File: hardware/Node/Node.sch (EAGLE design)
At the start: 67 parts, among them J1 AVR_SPI_PRG_6NS, J2 M04X2, Q1 PMR280UN, Q2 PMR280UN, Q3 PMR280UN, SW1 KSS, SW2 KSS, U1 ATMEGA32U4QFN, U2 BLUETOOTH-RN41", U3 LSM303DLM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

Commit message: move stuff to meet the DRC
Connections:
- net GND: now also HWB.3; no longer HWB.1
- net HWB: now also HWB.1; no longer HWB.3
- net PROG2: now also U1.PB7; no longer U1.PB0(SS)
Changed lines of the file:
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@@
 <instance part="SW1" gate="G$1" x="160.02" y="154.94" rot="MR0"/>
 <instance part="SW2" gate="G$1" x="160.02" y="144.78"/>
-<instance part="HWB" gate="G$1" x="48.26" y="134.62" smashed="yes">
-<attribute name="NAME" x="45.72" y="140.97" size="1.778" layer="95"/>
+<instance part="HWB" gate="G$1" x="48.26" y="134.62" smashed="yes" rot="MR0">
+<attribute name="NAME" x="50.8" y="140.97" size="1.778" layer="95" rot="MR0"/>
 </instance>
 <instance part="POWER" gate="1" x="129.54" y="187.96"/>
@@
 <junction x="66.04" y="127"/>
 <wire x1="30.48" y1="127" x2="43.18" y2="127" width="0.1524" layer="91"/>
-<pinref part="HWB" gate="G$1" pin="1"/>
+<pinref part="HWB" gate="G$1" pin="3"/>
 <wire x1="43.18" y1="127" x2="66.04" y2="127" width="0.1524" layer="91"/>
 <wire x1="43.18" y1="134.62" x2="43.18" y2="127" width="0.1524" layer="91"/>
@@
 <segment>
 <wire x1="58.42" y1="134.62" x2="55.88" y2="134.62" width="0.1524" layer="91"/>
-<pinref part="HWB" gate="G$1" pin="3"/>
 <label x="55.88" y="134.62" size="1.778" layer="95"/>
 <pinref part="R18" gate="G$1" pin="1"/>
-<wire x1="55.88" y1="134.62" x2="53.34" y2="134.62" width="0.1524" layer="91"/>
+<pinref part="HWB" gate="G$1" pin="1"/>
+<wire x1="53.34" y1="134.62" x2="55.88" y2="134.62" width="0.1524" layer="91"/>
 <junction x="55.88" y="134.62"/>
 </segment>
@@
 </segment>
 <segment>
-<pinref part="U1" gate="G$1" pin="PB0(SS)"/>
-<wire x1="139.7" y1="76.2" x2="144.78" y2="76.2" width="0.1524" layer="91"/>
-<label x="144.78" y="76.2" size="1.778" layer="95"/>
-</segment>
-</net>
+<pinref part="U1" gate="G$1" pin="PB7"/>
+<wire x1="139.7" y1="83.82" x2="144.78" y2="83.82" width="0.1524" layer="91"/>
+<label x="144.78" y="83.82" size="1.778" layer="95"/>
+</segment>
+</net>

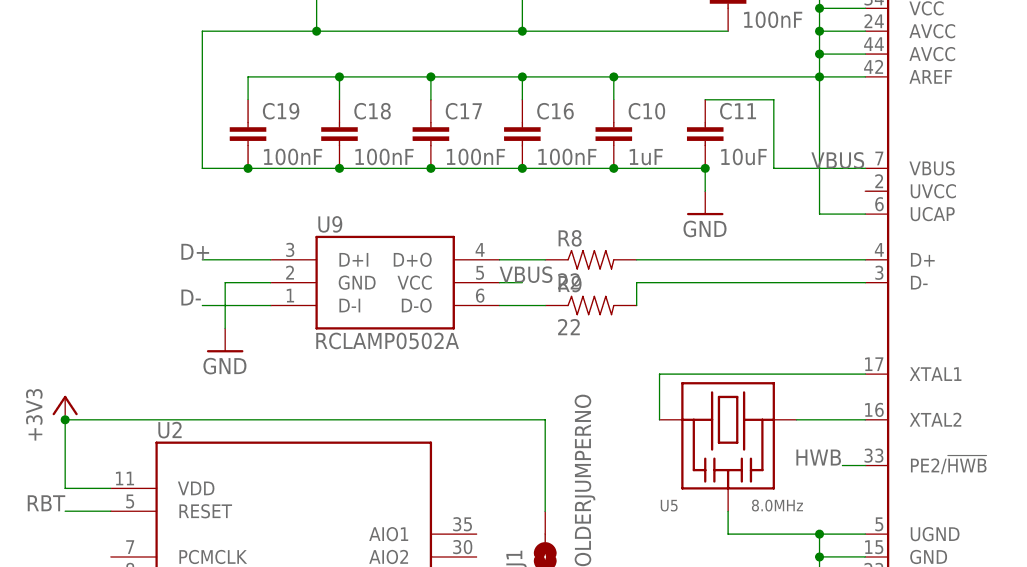
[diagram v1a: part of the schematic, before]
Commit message: fix packages, route ISP
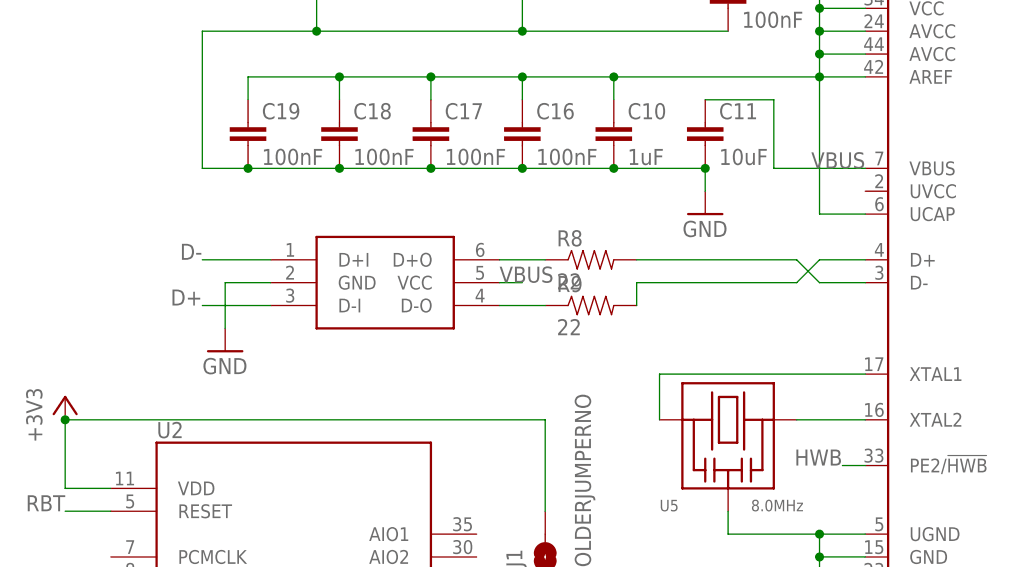
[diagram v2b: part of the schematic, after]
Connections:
- removed net N$23: R8.2, U1.D+
- new net N$15: R8.2, U1.D-
- net D+: now also U9.D-I; no longer U9.D+I
- net D-: now also U9.D+I; no longer U9.D-I
- net N$24: now also U1.D+; no longer U1.D-
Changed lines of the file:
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@@
 </segment>
 </net>
-<net name="N$23" class="0">
-<segment>
-<pinref part="R8" gate="G$1" pin="2"/>
+<net name="N$24" class="0">
+<segment>
+<pinref part="R9" gate="G$1" pin="2"/>
+<wire x1="78.74" y1="99.06" x2="78.74" y2="96.52" width="0.1524" layer="91"/>
+<wire x1="78.74" y1="99.06" x2="96.52" y2="99.06" width="0.1524" layer="91"/>
+<wire x1="96.52" y1="99.06" x2="99.06" y2="101.6" width="0.1524" layer="91"/>
 <pinref part="U1" gate="G$1" pin="D+"/>
-<wire x1="78.74" y1="101.6" x2="104.14" y2="101.6" width="0.1524" layer="91"/>
-</segment>
-</net>
-<net name="N$24" class="0">
-<segment>
-<pinref part="U1" gate="G$1" pin="D-"/>
-<pinref part="R9" gate="G$1" pin="2"/>
-<wire x1="104.14" y1="99.06" x2="78.74" y2="99.06" width="0.1524" layer="91"/>
-<wire x1="78.74" y1="99.06" x2="78.74" y2="96.52" width="0.1524" layer="91"/>
+<wire x1="99.06" y1="101.6" x2="104.14" y2="101.6" width="0.1524" layer="91"/>
 </segment>
 </net>
@@
 </segment>
 <segment>
-<wire x1="38.1" y1="96.52" x2="30.48" y2="96.52" width="0.1524" layer="91"/>
-<label x="27.94" y="96.52" size="1.778" layer="95"/>
-<pinref part="U9" gate="G$1" pin="D-I"/>
+<pinref part="U9" gate="G$1" pin="D+I"/>
+<wire x1="38.1" y1="101.6" x2="30.48" y2="101.6" width="0.1524" layer="91"/>
+<label x="30.48" y="101.6" size="1.778" layer="95" rot="MR0"/>
 </segment>
 </net>
@@
 </segment>
 <segment>
-<wire x1="38.1" y1="101.6" x2="30.48" y2="101.6" width="0.1524" layer="91"/>
-<label x="27.94" y="101.6" size="1.778" layer="95"/>
-<pinref part="U9" gate="G$1" pin="D+I"/>
+<pinref part="U9" gate="G$1" pin="D-I"/>
+<wire x1="38.1" y1="96.52" x2="30.48" y2="96.52" width="0.1524" layer="91"/>
+<label x="30.48" y="96.52" size="1.778" layer="95" rot="MR0"/>
 </segment>
 </net>
@@
 </segment>
 </net>
+<net name="N$15" class="0">
+<segment>
+<pinref part="R8" gate="G$1" pin="2"/>
+<wire x1="78.74" y1="101.6" x2="96.52" y2="101.6" width="0.1524" layer="91"/>
+<wire x1="96.52" y1="101.6" x2="99.06" y2="99.06" width="0.1524" layer="91"/>
+<pinref part="U1" gate="G$1" pin="D-"/>
+<wire x1="99.06" y1="99.06" x2="104.14" y2="99.06" width="0.1524" layer="91"/>
+</segment>
+</net>

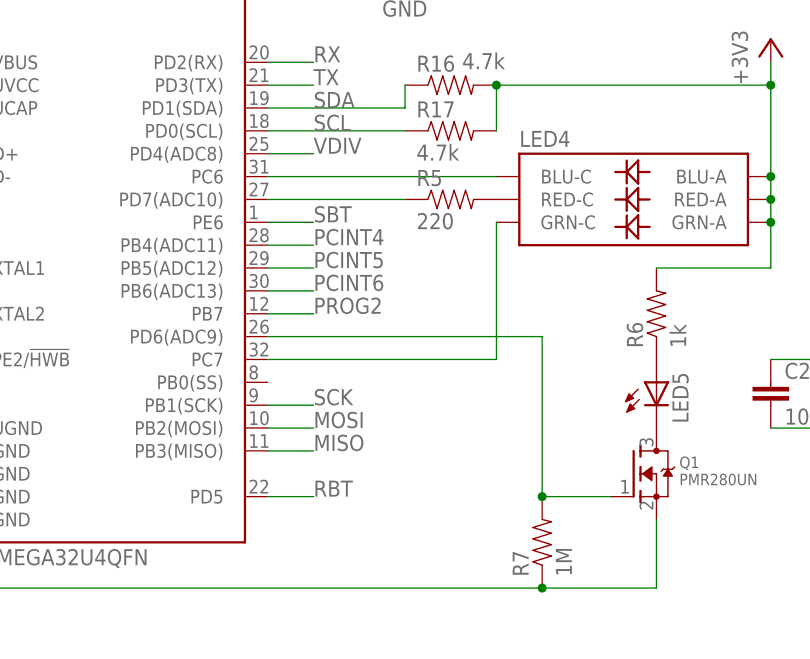
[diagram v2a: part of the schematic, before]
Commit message: route LEDs and interrupts
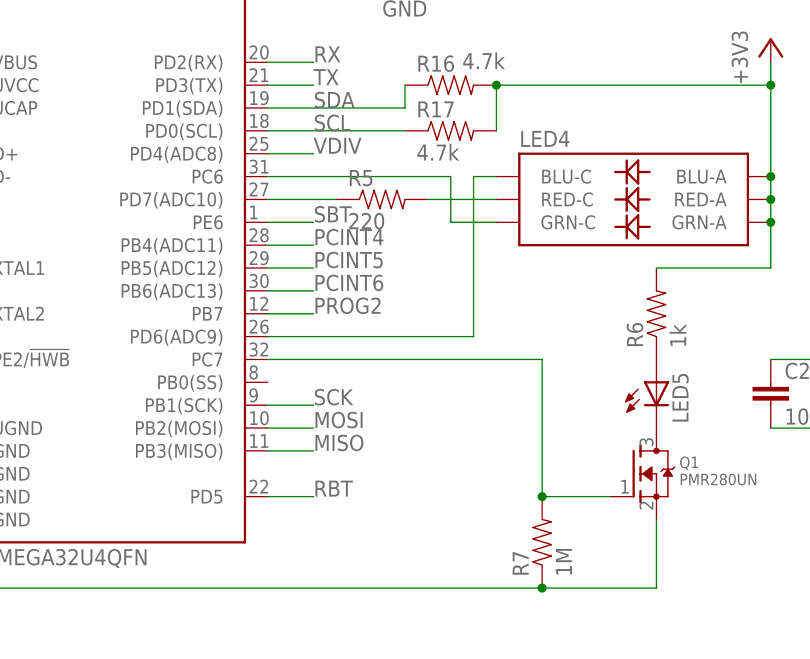
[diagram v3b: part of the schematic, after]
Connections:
- net N$12: now also LED4.GRN-C; no longer LED4.BLU-C
- net N$17: now also LED4.BLU-C, U1.PD6(ADC9); no longer LED4.GRN-C, U1.PC7
- net N$22: now also U1.PC7; no longer U1.PD6(ADC9)
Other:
- moved on the sheet: R5
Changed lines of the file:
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@@
 <grid distance="0.1" unitdist="inch" unit="inch" style="lines" multiple="1" display="no" altdistance="0.01" altunitdist="inch" altunit="inch"/>
 <layers>
-<layer number="1" name="Top" color="4" fill="1" visible="no" active="no"/>
-<layer number="16" name="Bottom" color="1" fill="1" visible="no" active="no"/>
-<layer number="17" name="Pads" color="2" fill="1" visible="no" active="no"/>
-<layer number="18" name="Vias" color="2" fill="1" visible="no" active="no"/>
-<layer number="19" name="Unrouted" color="6" fill="1" visible="no" active="no"/>
-<layer number="20" name="Dimension" color="15" fill="1" visible="no" active="no"/>
-<layer number="21" name="tPlace" color="7" fill="1" visible="no" active="no"/>
-<layer number="22" name="bPlace" color="7" fill="1" visible="no" active="no"/>
-<layer number="23" name="tOrigins" color="15" fill="1" visible="no" active="no"/>
-<layer number="24" name="bOrigins" color="15" fill="1" visible="no" active="no"/>
-<layer number="25" name="tNames" color="7" fill="1" visible="no" active="no"/>
-<layer number="26" name="bNames" color="7" fill="1" visible="no" active="no"/>
-<layer number="27" name="tValues" color="7" fill="1" visible="no" active="no"/>
-<layer number="28" name="bValues" color="7" fill="1" visible="no" active="no"/>
+<layer number="1" name="Top" color="4" fill="1" visible="yes" active="no"/>
+<layer number="16" name="Bottom" color="1" fill="1" visible="yes" active="no"/>
+<layer number="17" name="Pads" color="2" fill="1" visible="yes" active="no"/>
+<layer number="18" name="Vias" color="2" fill="1" visible="yes" active="no"/>
+<layer number="19" name="Unrouted" color="6" fill="1" visible="yes" active="no"/>
+<layer number="20" name="Dimension" color="15" fill="1" visible="yes" active="no"/>
+<layer number="21" name="tPlace" color="7" fill="1" visible="yes" active="no"/>
+<layer number="22" name="bPlace" color="7" fill="1" visible="yes" active="no"/>
+<layer number="23" name="tOrigins" color="15" fill="1" visible="yes" active="no"/>
+<layer number="24" name="bOrigins" color="15" fill="1" visible="yes" active="no"/>
+<layer number="25" name="tNames" color="7" fill="1" visible="yes" active="no"/>
+<layer number="26" name="bNames" color="7" fill="1" visible="yes" active="no"/>
+<layer number="27" name="tValues" color="7" fill="1" visible="yes" active="no"/>
+<layer number="28" name="bValues" color="7" fill="1" visible="yes" active="no"/>
 <layer number="29" name="tStop" color="7" fill="3" visible="no" active="no"/>
 <layer number="30" name="bStop" color="7" fill="6" visible="no" active="no"/>
@@
 <layer number="35" name="tGlue" color="7" fill="4" visible="no" active="no"/>
 <layer number="36" name="bGlue" color="7" fill="5" visible="no" active="no"/>
-<layer number="37" name="tTest" color="7" fill="1" visible="no" active="no"/>
-<layer number="38" name="bTest" color="7" fill="1" visible="no" active="no"/>
+<layer number="37" name="tTest" color="7" fill="1" visible="yes" active="no"/>
+<layer number="38" name="bTest" color="7" fill="1" visible="yes" active="no"/>
 <layer number="39" name="tKeepout" color="4" fill="11" visible="no" active="no"/>
 <layer number="40" name="bKeepout" color="1" fill="11" visible="no" active="no"/>
@@
 <layer number="44" name="Drills" color="7" fill="1" visible="no" active="no"/>
 <layer number="45" name="Holes" color="7" fill="1" visible="no" active="no"/>
-<layer number="46" name="Milling" color="3" fill="1" visible="no" active="no"/>
-<layer number="47" name="Measures" color="7" fill="1" visible="no" active="no"/>
-<layer number="48" name="Document" color="7" fill="1" visible="no" active="no"/>
-<layer number="49" name="Reference" color="7" fill="1" visible="no" active="no"/>
-<layer number="50" name="dxf" color="7" fill="1" visible="no" active="no"/>
-<layer number="51" name="tDocu" color="7" fill="1" visible="no" active="no"/>
-<layer number="52" name="bDocu" color="7" fill="1" visible="no" active="no"/>
-<layer number="53" name="tGND_GNDA" color="7" fill="9" visible="no" active="no"/>
-<layer number="54" name="bGND_GNDA" color="1" fill="9" visible="no" active="no"/>
-<layer number="56" name="wert" color="7" fill="1" visible="no" active="no"/>
+<layer number="46" name="Milling" color="3" fill="1" visible="yes" active="no"/>
+<layer number="47" name="Measures" color="7" fill="1" visible="yes" active="no"/>
+<layer number="48" name="Document" color="7" fill="1" visible="yes" active="no"/>
+<layer number="49" name="Reference" color="7" fill="1" visible="yes" active="no"/>
+<layer number="50" name="dxf" color="7" fill="1" visible="yes" active="no"/>
+<layer number="51" name="tDocu" color="7" fill="1" visible="yes" active="no"/>
+<layer number="52" name="bDocu" color="7" fill="1" visible="yes" active="no"/>
+<layer number="53" name="tGND_GNDA" color="7" fill="9" visible="yes" active="no"/>
+<layer number="54" name="bGND_GNDA" color="1" fill="9" visible="yes" active="no"/>
+<layer number="56" name="wert" color="7" fill="1" visible="yes" active="no"/>
 <layer number="91" name="Nets" color="2" fill="1" visible="yes" active="yes"/>
 <layer number="92" name="Busses" color="1" fill="1" visible="yes" active="yes"/>
@@
 <attribute name="NAME" x="167.64" y="102.362" size="1.778" layer="95"/>
 </instance>
-<instance part="R5" gate="G$1" x="160.02" y="96.52"/>
+<instance part="R5" gate="G$1" x="152.4" y="96.52"/>
 <instance part="+3V5" gate="G$1" x="195.58" y="114.3"/>
 <instance part="U7" gate="G$1" x="195.58" y="190.5"/>
@@
 </segment>
 </net>
-<net name="N$17" class="0">
-<segment>
-<pinref part="LED4" gate="G$1" pin="GRN-C"/>
-<wire x1="165.1" y1="93.98" x2="165.1" y2="78.74" width="0.1524" layer="91"/>
-<pinref part="U1" gate="G$1" pin="PC7"/>
-<wire x1="165.1" y1="78.74" x2="139.7" y2="78.74" width="0.1524" layer="91"/>
-</segment>
-</net>
 <net name="N$18" class="0">
 <segment>
 <pinref part="U1" gate="G$1" pin="PD7(ADC10)"/>
-<wire x1="154.94" y1="96.52" x2="139.7" y2="96.52" width="0.1524" layer="91"/>
+<wire x1="147.32" y1="96.52" x2="139.7" y2="96.52" width="0.1524" layer="91"/>
 <pinref part="R5" gate="G$1" pin="1"/>
 </segment>
@@
 <pinref part="R7" gate="G$1" pin="2"/>
 <wire x1="177.8" y1="63.5" x2="170.18" y2="63.5" width="0.1524" layer="91"/>
-<wire x1="170.18" y1="63.5" x2="170.18" y2="81.28" width="0.1524" layer="91"/>
+<wire x1="170.18" y1="63.5" x2="170.18" y2="78.74" width="0.1524" layer="91"/>
 <junction x="170.18" y="63.5"/>
-<pinref part="U1" gate="G$1" pin="PD6(ADC9)"/>
-<wire x1="170.18" y1="81.28" x2="139.7" y2="81.28" width="0.1524" layer="91"/>
 <pinref part="Q1" gate="G$1" pin="G"/>
+<pinref part="U1" gate="G$1" pin="PC7"/>
+<wire x1="170.18" y1="78.74" x2="139.7" y2="78.74" width="0.1524" layer="91"/>
 </segment>
 </net>
@@
 <pinref part="R5" gate="G$1" pin="2"/>
 <pinref part="LED4" gate="G$1" pin="RED-C"/>
-</segment>
-</net>
-<net name="N$12" class="0">
-<segment>
-<pinref part="U1" gate="G$1" pin="PC6"/>
-<wire x1="165.1" y1="99.06" x2="139.7" y2="99.06" width="0.1524" layer="91"/>
-<pinref part="LED4" gate="G$1" pin="BLU-C"/>
+<wire x1="157.48" y1="96.52" x2="165.1" y2="96.52" width="0.1524" layer="91"/>
 </segment>
 </net>
@@
 </segment>
 </net>
+<net name="N$12" class="0">
+<segment>
+<pinref part="LED4" gate="G$1" pin="GRN-C"/>
+<wire x1="165.1" y1="93.98" x2="160.02" y2="93.98" width="0.1524" layer="91"/>
+<wire x1="160.02" y1="93.98" x2="160.02" y2="99.06" width="0.1524" layer="91"/>
+<pinref part="U1" gate="G$1" pin="PC6"/>
+<wire x1="160.02" y1="99.06" x2="139.7" y2="99.06" width="0.1524" layer="91"/>
+</segment>
+</net>
+<net name="N$17" class="0">
+<segment>
+<pinref part="LED4" gate="G$1" pin="BLU-C"/>
+<wire x1="165.1" y1="99.06" x2="162.56" y2="99.06" width="0.1524" layer="91"/>
+<wire x1="162.56" y1="99.06" x2="162.56" y2="81.28" width="0.1524" layer="91"/>
+<pinref part="U1" gate="G$1" pin="PD6(ADC9)"/>
+<wire x1="162.56" y1="81.28" x2="139.7" y2="81.28" width="0.1524" layer="91"/>
+</segment>
+</net>
